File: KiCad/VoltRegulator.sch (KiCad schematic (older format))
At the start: 11 parts, among them P7 CONN_01X02, U2 LM317, U3 LM317

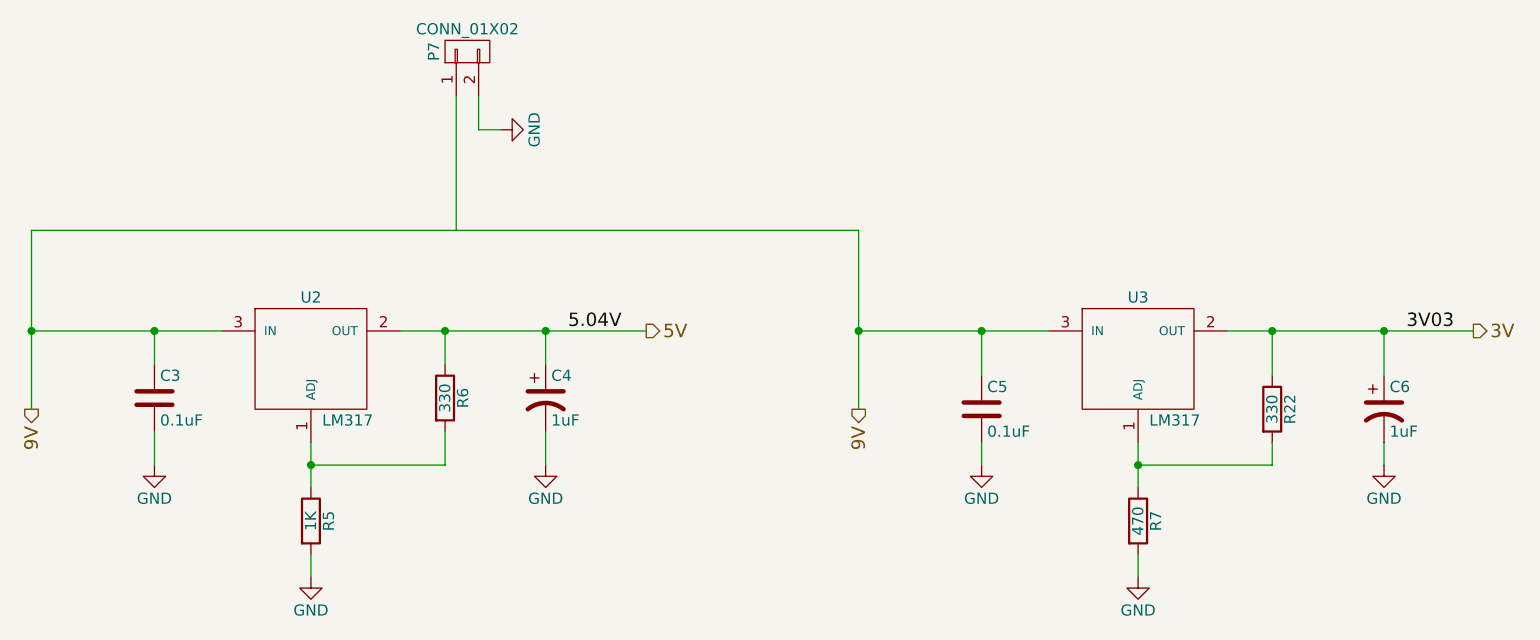
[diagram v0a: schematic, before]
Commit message: Updated the pcb to smaller size and footprints
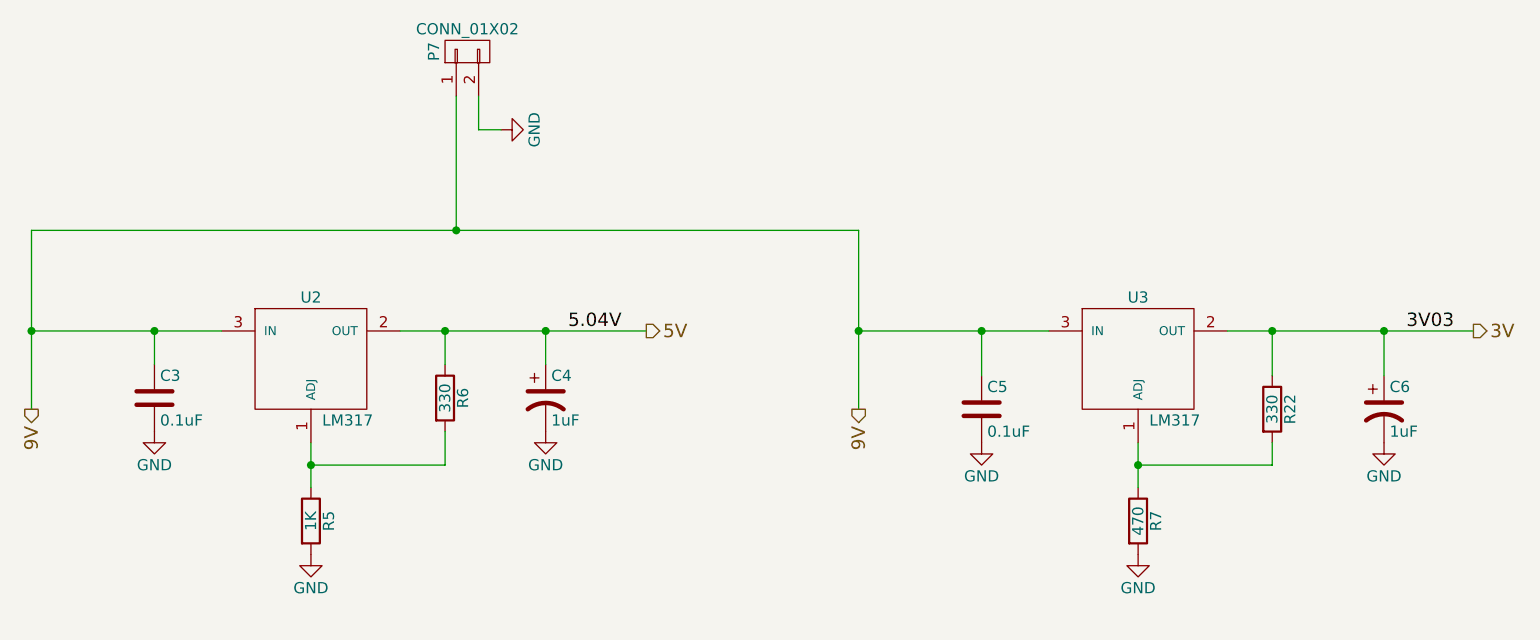
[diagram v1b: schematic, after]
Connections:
- net 9V: now also P7.1 (P1)
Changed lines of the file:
@@
 5V
 $Comp
-L GND #PWR08
+L GND #PWR010
 U 1 1 571613A6
-P 4050 3550
-F 0 "#PWR08" H 4050 3300 50  0001 C CNN
-F 1 "GND" H 4050 3400 50  0000 C CNN
-F 2 "" H 4050 3550 50  0000 C CNN
-F 3 "" H 4050 3550 50  0000 C CNN
-	1    4050 3550
+P 4050 3450
+F 0 "#PWR010" H 4050 3200 50  0001 C CNN
+F 1 "GND" H 4050 3300 50  0000 C CNN
+F 2 "" H 4050 3450 50  0000 C CNN
+F 3 "" H 4050 3450 50  0000 C CNN
+	1    4050 3450
 	1    0    0    -1
 $EndComp
@@
 3V
 $Comp
-L GND #PWR09
+L GND #PWR011
 U 1 1 571810D3
-P 7750 3550
-F 0 "#PWR09" H 7750 3300 50  0001 C CNN
-F 1 "GND" H 7750 3400 50  0000 C CNN
-F 2 "" H 7750 3550 50  0000 C CNN
-F 3 "" H 7750 3550 50  0000 C CNN
-	1    7750 3550
+P 7750 3450
+F 0 "#PWR011" H 7750 3200 50  0001 C CNN
+F 1 "GND" H 7750 3300 50  0000 C CNN
+F 2 "" H 7750 3450 50  0000 C CNN
+F 3 "" H 7750 3450 50  0000 C CNN
+	1    7750 3450
 	1    0    0    -1
 $EndComp
@@
 Connection ~ 7750 3050
 Wire Wire Line
-	7750 3450 7750 3550
-Wire Wire Line
 	4650 2450 4650 2600
 Connection ~ 4650 2450
@@
 	4050 2950 4050 3150
 Connection ~ 4050 3050
-Wire Wire Line
-	4050 3450 4050 3550
 $Comp
 L CP1 C4
@@
 	5100 2600 5100 2450
 Connection ~ 5100 2450
-Wire Wire Line
-	5100 2900 5100 3050
-Wire Wire Line
-	8850 2950 8850 3050
 $Comp
 L C C3
@@
 Connection ~ 7050 2450
 Wire Wire Line
-	7050 2950 7050 3050
-Wire Wire Line
 	3350 2600 3350 2450
 Connection ~ 3350 2450
-Wire Wire Line
-	3350 2900 3350 3050
-$Comp
-L GND #PWR010
+$Comp
+L GND #PWR012
 U 1 1 571BC1AC
-P 3350 3050
-F 0 "#PWR010" H 3350 2800 50  0001 C CNN
-F 1 "GND" H 3350 2900 50  0000 C CNN
-F 2 "" H 3350 3050 50  0000 C CNN
-F 3 "" H 3350 3050 50  0000 C CNN
-	1    3350 3050
-	1    0    0    -1
-$EndComp
-$Comp
-L GND #PWR011
+P 3350 2900
+F 0 "#PWR012" H 3350 2650 50  0001 C CNN
+F 1 "GND" H 3350 2750 50  0000 C CNN
+F 2 "" H 3350 2900 50  0000 C CNN
+F 3 "" H 3350 2900 50  0000 C CNN
+	1    3350 2900
+	1    0    0    -1
+$EndComp
+$Comp
+L GND #PWR013
 U 1 1 571BC2DA
-P 5100 3050
-F 0 "#PWR011" H 5100 2800 50  0001 C CNN
-F 1 "GND" H 5100 2900 50  0000 C CNN
-F 2 "" H 5100 3050 50  0000 C CNN
-F 3 "" H 5100 3050 50  0000 C CNN
-	1    5100 3050
-	1    0    0    -1
-$EndComp
-$Comp
-L GND #PWR012
+P 5100 2900
+F 0 "#PWR013" H 5100 2650 50  0001 C CNN
+F 1 "GND" H 5100 2750 50  0000 C CNN
+F 2 "" H 5100 2900 50  0000 C CNN
+F 3 "" H 5100 2900 50  0000 C CNN
+	1    5100 2900
+	1    0    0    -1
+$EndComp
+$Comp
+L GND #PWR014
 U 1 1 571BC41B
-P 7050 3050
-F 0 "#PWR012" H 7050 2800 50  0001 C CNN
-F 1 "GND" H 7050 2900 50  0000 C CNN
-F 2 "" H 7050 3050 50  0000 C CNN
-F 3 "" H 7050 3050 50  0000 C CNN
-	1    7050 3050
-	1    0    0    -1
-$EndComp
-$Comp
-L GND #PWR013
+P 7050 2950
+F 0 "#PWR014" H 7050 2700 50  0001 C CNN
+F 1 "GND" H 7050 2800 50  0000 C CNN
+F 2 "" H 7050 2950 50  0000 C CNN
+F 3 "" H 7050 2950 50  0000 C CNN
+	1    7050 2950
+	1    0    0    -1
+$EndComp
+$Comp
+L GND #PWR015
 U 1 1 571BC444
-P 8850 3050
-F 0 "#PWR013" H 8850 2800 50  0001 C CNN
-F 1 "GND" H 8850 2900 50  0000 C CNN
-F 2 "" H 8850 3050 50  0000 C CNN
-F 3 "" H 8850 3050 50  0000 C CNN
-	1    8850 3050
+P 8850 2950
+F 0 "#PWR015" H 8850 2700 50  0001 C CNN
+F 1 "GND" H 8850 2800 50  0000 C CNN
+F 2 "" H 8850 2950 50  0000 C CNN
+F 3 "" H 8850 2950 50  0000 C CNN
+	1    8850 2950
 	1    0    0    -1
 $EndComp
@@
 	2800 2000 6500 2000
 Wire Wire Line
-	4700 1400 4700 2000
-Wire Wire Line
 	4800 1400 4800 1550
 Wire Wire Line
 	4800 1550 4900 1550
 $Comp
-L GND #PWR014
+L GND #PWR016
 U 1 1 5735CD07
 P 4900 1550
-F 0 "#PWR014" H 4900 1300 50  0001 C CNN
+F 0 "#PWR016" H 4900 1300 50  0001 C CNN
 F 1 "GND" H 4900 1400 50  0000 C CNN
 F 2 "" H 4900 1550 50  0000 C CNN
@@
 	0    -1   -1   0
 $EndComp
+Wire Wire Line
+	4700 1400 4700 2000
+Connection ~ 4700 2000
 $EndSCHEMATC
